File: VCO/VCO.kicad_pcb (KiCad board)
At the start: 2 copper layers, 22 parts, among them J1 JACK_STEREO, Q1 Q_NMOS_SGD, SW1 SWITCH_INV, U1 LM324

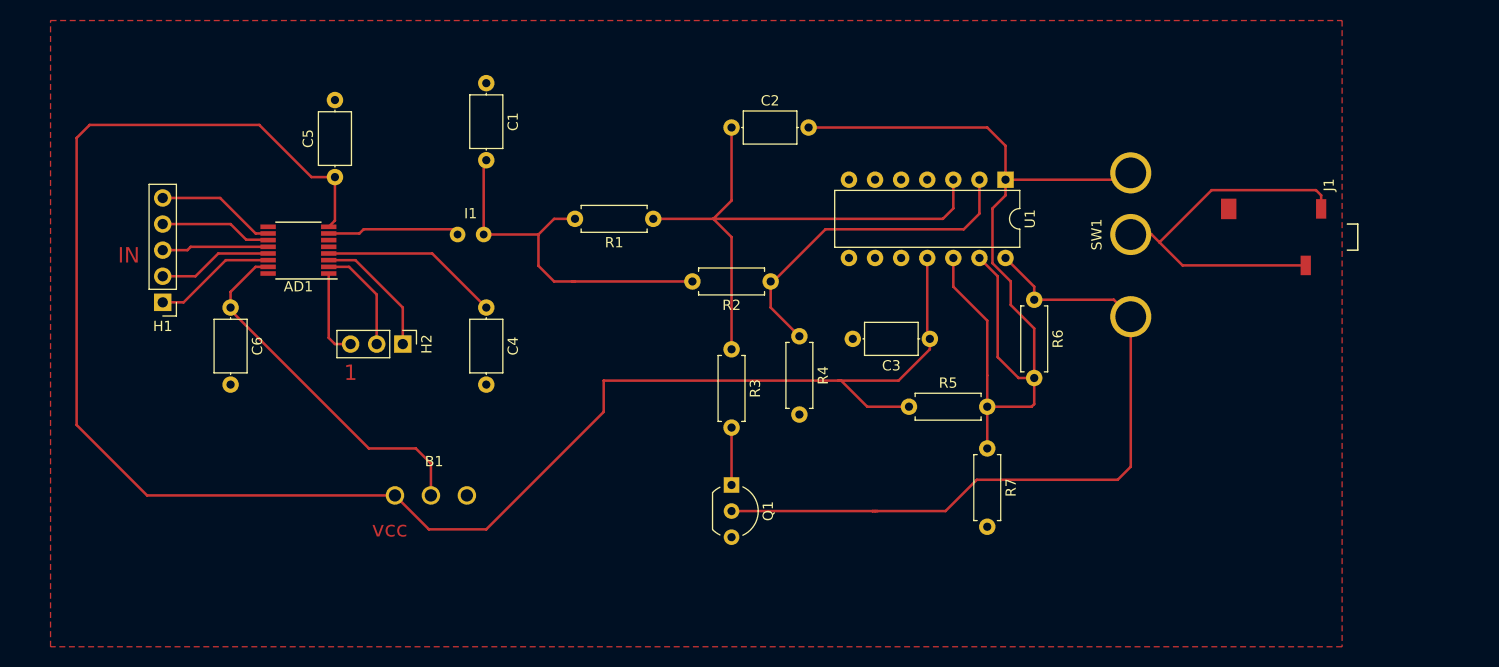
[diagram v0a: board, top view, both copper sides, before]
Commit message: Fixed AO power
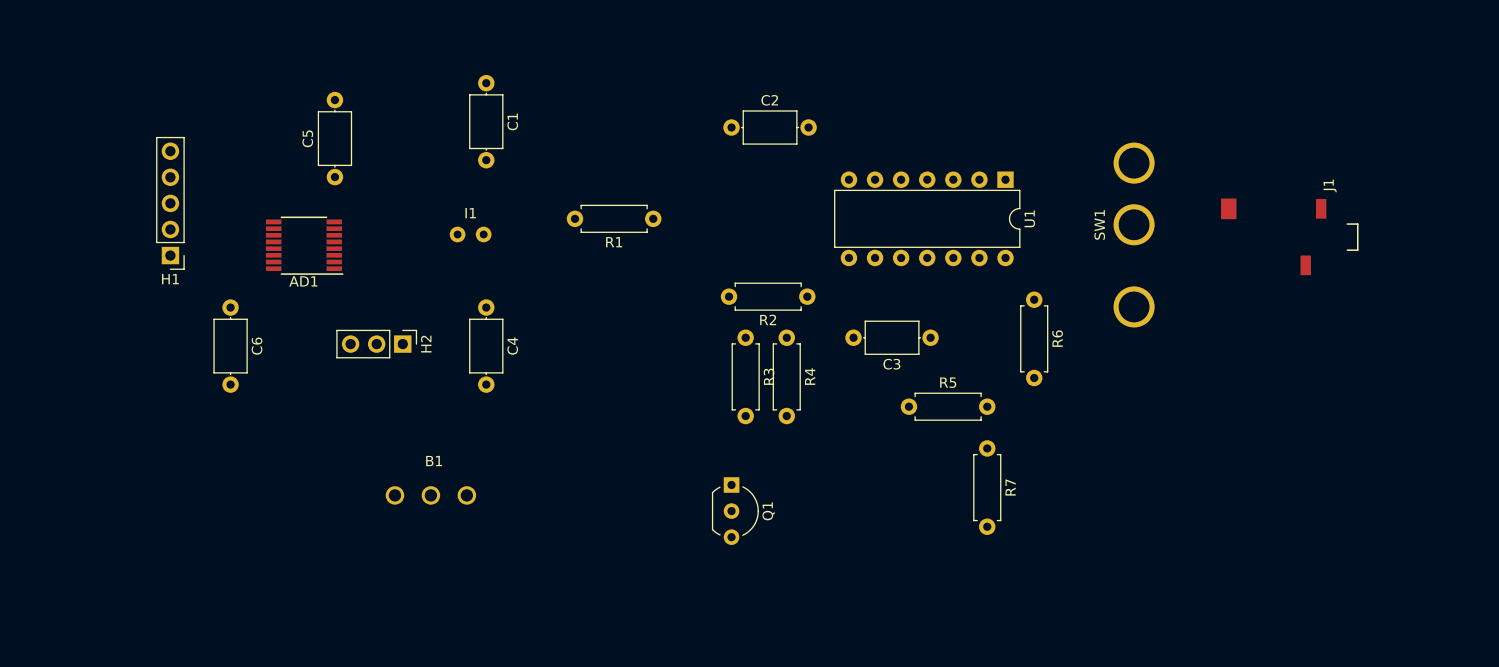
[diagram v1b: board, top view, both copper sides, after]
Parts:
- moved H1 4.61 mm to (112.0, 94.0)
- moved R2 3.86 mm to (174.0, 98.0)
- moved R3 1.78 mm to (168.0, 102.0)
- moved R4 1.24 mm to (172.0, 102.0)
- moved SW1 1.00 mm to (202.0, 91.0)
- moved AD1 0.72 mm to (125.0, 93.0)
- moved C3 0.13 mm to (186.0, 102.0)
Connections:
- AD1 pad 9: Net-(AD1-Pad9) -> (no net)
- U1 pad 11: VCC -> GND
- U1 pad 4: GND -> VCC
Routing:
- net VCC: track 174.0 -> 0.00 mm
- net Net-(C2-Pad2): track 99.1 -> 0.00 mm
- net Net-(Q1-Pad2): track 71.1 -> 0.00 mm
- net Net-(C2-Pad1): track 55.5 -> 0.00 mm
- net Net-(J1-Pad2): track 37.7 -> 0.00 mm
- net Net-(C1-Pad2): track 35.8 -> 0.00 mm
- net VDD: track 35.2 -> 0.00 mm
- net Net-(R2-Pad1): track 32.8 -> 0.00 mm
- net Net-(AD1-Pad4): track 17.5 -> 0.00 mm
- net Net-(AD1-Pad7): track 13.1 -> 0.00 mm
- net /~RESET: track 12.7 -> 0.00 mm
- net /SCLK: track 12.0 -> 0.00 mm
- net /SDO: track 11.7 -> 0.00 mm
- net /~SYNC: track 11.2 -> 0.00 mm
- net /~LDAC: track 10.9 -> 0.00 mm
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- removed copper zone on F.Cu, net GND
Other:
- net class Default: trace_width 0.25 -> 1
- board text removed: "1"
- board text removed: "IN"
- board text removed: "vcc"

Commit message: DCO final version
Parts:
- AD1: moved to B.Cu
- moved C3 50.1 mm to (135.9, 102.9), turned to 0 degrees
- moved R5 32.6 mm to (166.4, 81.3), turned to 180 degrees
- moved R2 19.1 mm to (154.9, 96.5)
- moved U1 18.1 mm to (175.3, 87.6), turned to 0 degrees
- moved R4 17.1 mm to (154.9, 100.3), turned to 180 degrees
- moved H2 15.0 mm to (135.9, 87.6), turned to 180 degrees
- moved C5 13.9 mm to (135.9, 97.8), turned to 0 degrees
- moved R3 13.1 mm to (158.8, 92.7)
- moved B1 10.9 mm to (139.7, 102.9)
- moved Q1 10.5 mm to (162.6, 106.7), turned to 0 degrees
- moved C6 10.3 mm to (119.4, 88.9), turned to 90 degrees
- moved C4 10.3 mm to (135.9, 91.4), turned to 0 degrees
- moved C1 10.2 mm to (147.3, 86.4), turned to 0 degrees
- moved C2 9.24 mm to (158.8, 86.4)
- moved R7 8.99 mm to (198.1, 106.7), turned to 180 degrees
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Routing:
- net Net-(C2-Pad2): track 0.00 -> 101.4 mm
- net VCC: track 0.00 -> 82.4 mm
- net Net-(Q1-Pad2): track 0.00 -> 81.7 mm
- net VDD: track 0.00 -> 42.1 mm
- net Net-(J1-Pad2): track 0.00 -> 37.6 mm
- net Net-(R2-Pad1): track 0.00 -> 29.0 mm
- net Net-(C2-Pad1): track 0.00 -> 28.2 mm
- net GND: track 0.00 -> 19.7 mm
- net Net-(C1-Pad2): track 0.00 -> 18.5 mm
- net Net-(AD1-Pad7): track 0.00 -> 15.6 mm
- net /~ALERT: track 0.00 -> 13.7 mm
- net /SDO: track 0.00 -> 13.4 mm
- net /SCLK: track 0.00 -> 12.9 mm
- net /~LDAC: track 0.00 -> 12.6 mm
- net /~SYNC: track 0.00 -> 12.1 mm
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- added copper zone on B.Cu, net GND
- added copper zone on F.Cu, net GND
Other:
- net class Default: trace_width 1 -> 0.25
- board text added: "C"
- board text added: "IN"
- board text added: "T"

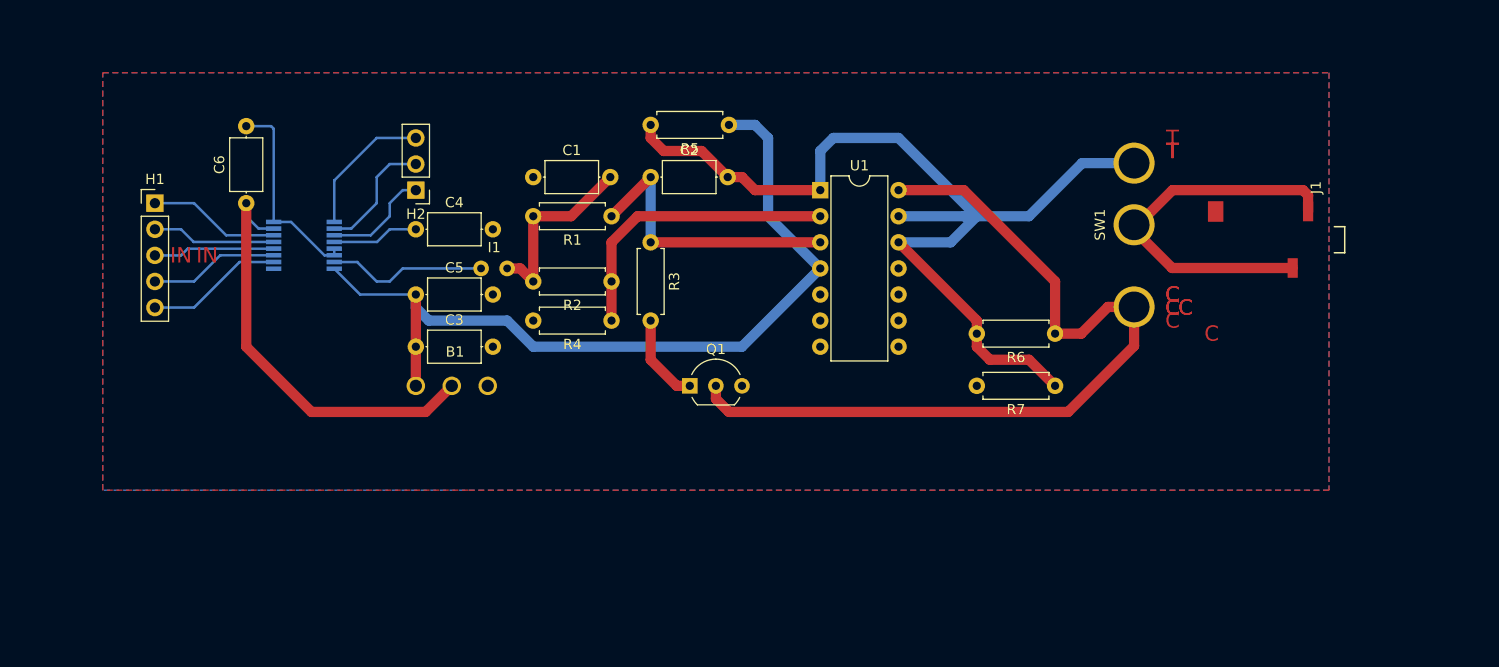
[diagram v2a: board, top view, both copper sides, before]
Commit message: Added labels and fixed routing
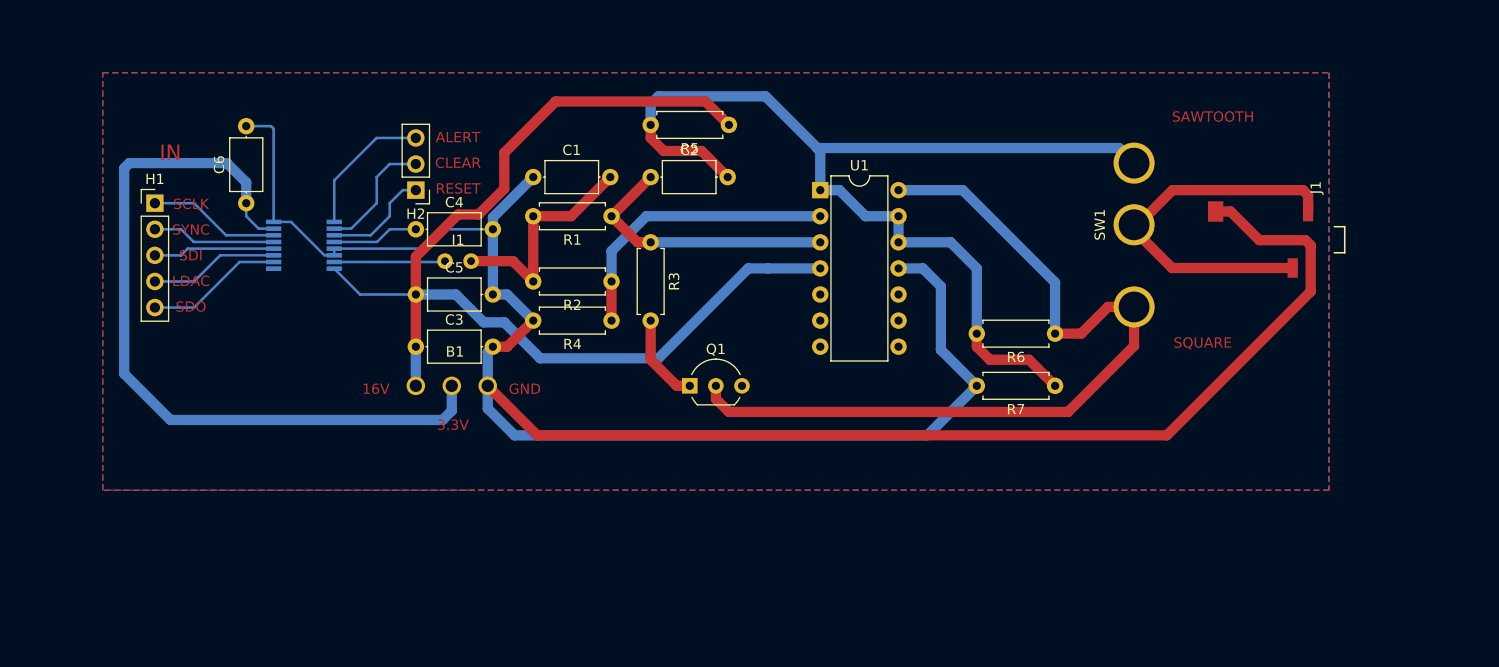
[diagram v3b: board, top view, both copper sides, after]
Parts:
- moved I1 3.58 mm to (140.0, 92.0)
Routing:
- net GND: track 19.7 -> 234.9 mm
- net VDD: track 42.1 -> 75.9 mm
- net VCC: track 82.4 -> 106.9 mm
- net Net-(AD1-Pad7): track 15.6 -> 10.8 mm
- net Net-(C1-Pad2): track 18.5 -> 22.3 mm
- net Net-(C2-Pad2): track 101.4 -> 103.4 mm
- net Net-(C2-Pad1): track 28.2 -> 26.8 mm
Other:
- net class Default: trace_width 0.25 -> 1
- board text added: "16V"
- board text added: "3.3V"
- board text added: "ALERT"
- board text added: "CLEAR"
- board text added: "GND"
- board text added: "LDAC"
- board text added: "RESET"
- board text added: "SAWTOOTH"
- board text added: "SCLK"
- board text added: "SDI"
- board text added: "SDO"
- board text added: "SQUARE"
- board text added: "SYNC"
- board text removed: "C"
- board text removed: "T"

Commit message: Fixed VCO
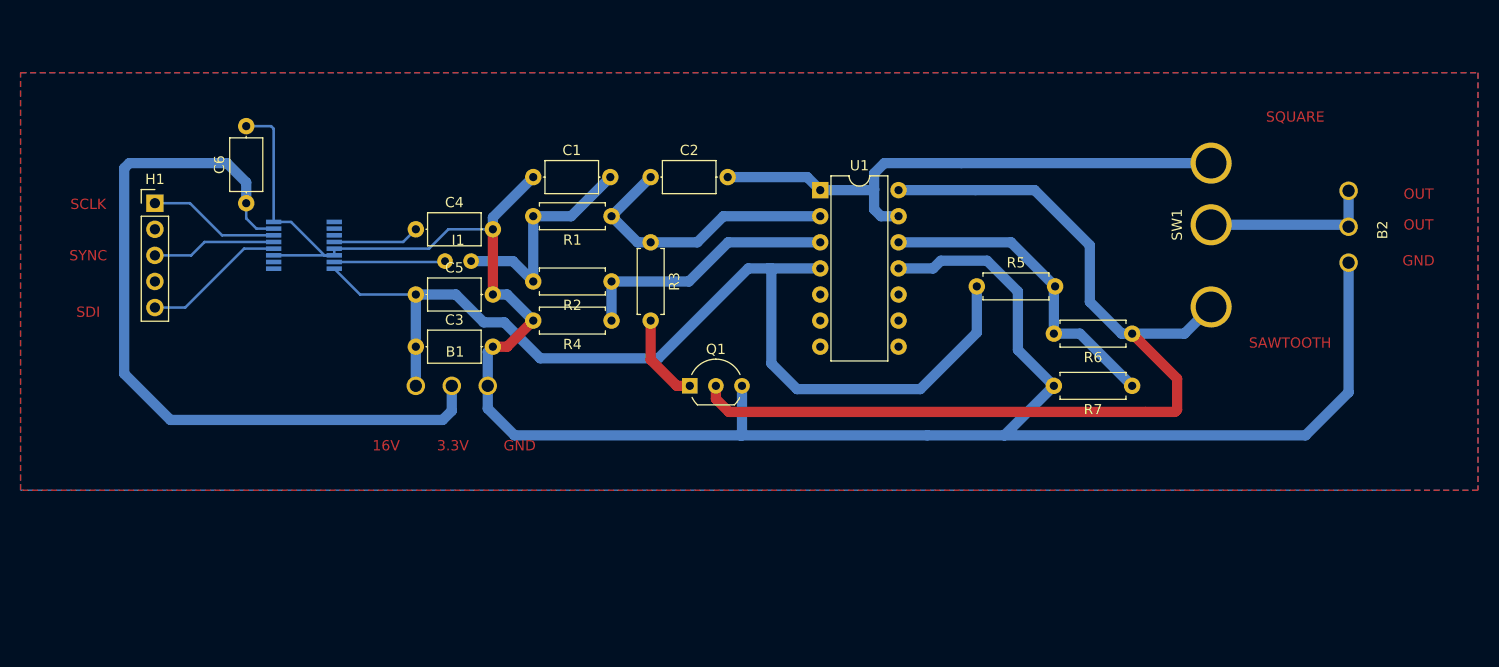
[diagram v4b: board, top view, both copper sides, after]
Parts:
- removed H2: Header_right, Pin_Headers:Pin_Header_Straight_1x03_Pitch2.54mm
- removed J1: JACK_STEREO, jack:jack-stereo
- added B2: Bornier_OUT, bornier:Bornier_3pins, F.Cu at (230.5, 91.5)
- moved R5 28.8 mm to (190.5, 97.0), turned to 0 degrees
- moved R6 7.50 mm to (205.6, 101.6)
- moved R7 7.50 mm to (205.6, 106.7)
- moved SW1 7.50 mm to (209.5, 91.0)
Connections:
- AD1 pad 1: /~ALERT -> (no net)
- AD1 pad 10: /SDO -> (no net)
- AD1 pad 11: /~LDAC -> GND
- AD1 pad 2: /~CLEAR -> (no net)
- AD1 pad 3: /~RESET -> (no net)
- H1 pad 2: /~SYNC -> (no net)
- H1 pad 3: /SDI -> /~SYNC
- H1 pad 4: /~LDAC -> (no net)
- H1 pad 5: /SDO -> /SDI
- R5 pad 2: Net-(C2-Pad2) -> Net-(R5-Pad2)
- R6 pad 2: Net-(C2-Pad2) -> Net-(R5-Pad2)
- R7 pad 1: Net-(C2-Pad2) -> Net-(R5-Pad2)
- U1 pad 12: Net-(C2-Pad2) -> Net-(R5-Pad2)
- U1 pad 2: Net-(R2-Pad1) -> Net-(C2-Pad1)
- U1 pad 3: Net-(C2-Pad1) -> Net-(R2-Pad1)
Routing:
- net Net-(C2-Pad2): track 103.4 -> 54.3 mm
- net Net-(R5-Pad2): track 0.00 -> 31.6 mm
- net GND: track 234.9 -> 205.9 mm
- net Net-(B2-Pad1): track 37.6 -> 17.2 mm
- net Net-(Q1-Pad2): track 81.7 -> 96.5 mm
- net /~ALERT: track 13.7 -> 0.00 mm
- net /SDO: track 13.4 -> 0.00 mm
- net /~LDAC: track 12.6 -> 0.00 mm
- net /~CLEAR: track 12.0 -> 0.00 mm
- net /~RESET: track 10.5 -> 0.00 mm
- net VCC: track 106.9 -> 100.5 mm
- net Net-(R2-Pad1): track 28.5 -> 25.7 mm
- net /SDI: track 11.8 -> 13.9 mm
- net Net-(C2-Pad1): track 26.8 -> 27.8 mm
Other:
- board text added: "OUT"
- board text removed: "ALERT"
- board text removed: "CLEAR"
- board text removed: "IN"
- board text removed: "LDAC"
- board text removed: "RESET"
- board text removed: "SDO"
